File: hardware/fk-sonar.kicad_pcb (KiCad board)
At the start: 2 copper layers, 28.4 x 70.3 mm, 72 parts, among them J1 Conn_01x03, J2 CONN-HDR-2x5, J3 RF-SMA-EDGE, J4 MICRO-USB, J5 S2B-PH-SM4-TB, J6 Conn_01x04, Q1 2N7002LT1G, Q2 2N7002LT1G, Q3 2N7002LT1G, Q4 2N7002LT1G, SW1 SPNO, U1 ATSAMD21G18A-AU, U2 RFM95W, U3 BQ24074RGTT, U4 S25FL116K0XMFI041, U5 MAX1704XX, U6 MCP1700T-3302E/MB, Y1 FC-135

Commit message: New SWD/JTAG programming footprint to avoid confusion.
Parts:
- added M1, M3, M4, M6: MOUNT_HOLE, RocketScreamKicadLibrary:HOLE_NPTH_2.2MM, F.Cu at (141.2, 187.0)
- added M2, M5: FIDUCIAL, RocketScreamKicadLibrary:FIDUCIAL-1MM, F.Cu at (141.2, 187.0)
- J2: footprint Socket_Strips:Socket_Strip_Straight_2x05_Pitch1.27mm_SMD -> conservify:HDR_2x5_Pitch1.27mm_SMD_JTAG_SWD
- moved J2 1.22 mm to (132.3, 119.7), turned to 180 degrees
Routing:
- net 3V3: track 221.8 -> 220.1 mm, vias 17 -> 18
- net GND: track 28.9 -> 27.6 mm
- net /SWDIO: track 20.7 -> 19.9 mm
- net /RST: track 42.9 -> 42.3 mm
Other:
- board text added: "SWD"

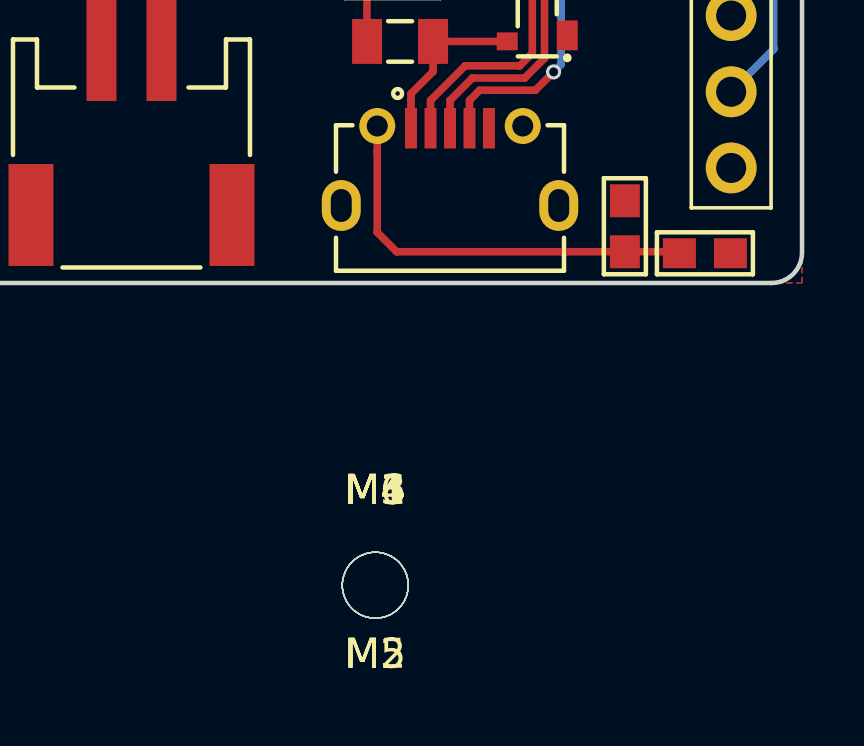
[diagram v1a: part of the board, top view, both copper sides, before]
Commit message: Using our MICRO-USB with the larger, non oval drills.
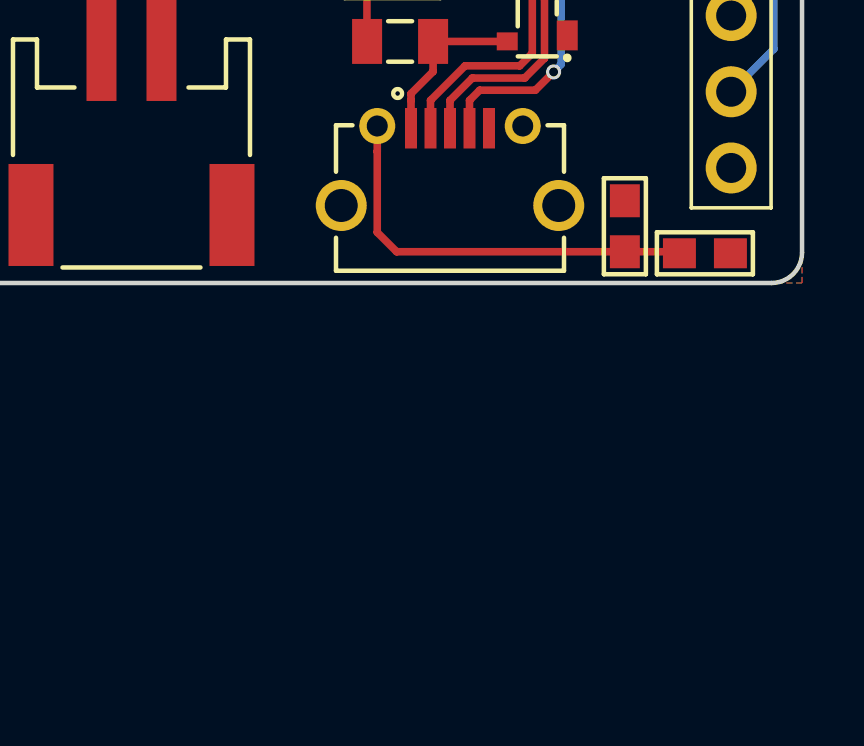
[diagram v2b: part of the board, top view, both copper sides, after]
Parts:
- removed M1, M3, M4, M6: MOUNT_HOLE, RocketScreamKicadLibrary:HOLE_NPTH_2.2MM
- removed M2, M5: FIDUCIAL, RocketScreamKicadLibrary:FIDUCIAL-1MM
- J4: footprint RocketScreamKicadLibrary:MICRO-USB -> conservify:MICRO-USB
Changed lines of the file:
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@@
     (links 179)
     (no_connects 61)
-    (area 118.588857 47.75 165.914286 191.092801)
+    (area 116.859486 47.75 165.914286 191.092801)
     (thickness 1.6)
     (drawings 15)
     (tracks 638)
     (zones 0)
-    (modules 78)
-    (nets 93)
+    (modules 72)
+    (nets 91)
   )
   (page A4)
@@
   (net 89 "Net-(U5-Pad5)")
   (net 90 "Net-(U5-Pad6)")
-  (net 91 "Net-(M2-Pad~)")
-  (net 92 "Net-(M5-Pad~)")
   (net_class Default "This is the default net class."
     (clearance 0.006)
@@
       (net 1 GND))
   )
-  (module RocketScreamKicadLibrary:MICRO-USB (layer F.Cu)
-    (at 143.7132 173.2534)
-    (tags MICRO-USB)
-    (fp_text reference J4 (at 0 -3.556) (layer F.SilkS) hide
-      (effects (font (size 1 1) (thickness 0.15)))
-    )
-    (fp_text value MICRO-USB (at 0 4.318) (layer F.Fab) hide
-      (effects (font (size 1 1) (thickness 0.15)))
-    )
-    (fp_line (start -4.55 -2.4) (end -4.55 3.45) (layer F.CrtYd) (width 0.05))
-    (fp_line (start -4.55 3.45) (end 4.55 3.45) (layer F.CrtYd) (width 0.05))
-    (fp_line (start 4.55 3.45) (end 4.55 -2.4) (layer F.CrtYd) (width 0.05))
-    (fp_line (start 4.55 -2.4) (end -4.55 -2.4) (layer F.CrtYd) (width 0.05))
-    (fp_circle (center -1.746 -2.608) (end -1.796 -2.658) (layer F.SilkS) (width 0.3))
-    (fp_line (start 3.8 0) (end 3.8 -1.55) (layer F.SilkS) (width 0.15))
-    (fp_line (start 3.8 -1.55) (end 3.25 -1.55) (layer F.SilkS) (width 0.15))
-    (fp_line (start -3.8 0) (end -3.8 -1.55) (layer F.SilkS) (width 0.15))
-    (fp_line (start -3.8 -1.55) (end -3.25 -1.55) (layer F.SilkS) (width 0.15))
-    (fp_line (start 3.8 2.2) (end 3.8 3.3) (layer F.SilkS) (width 0.15))
-    (fp_line (start -3.8 3.3) (end -3.8 2.2) (layer F.SilkS) (width 0.15))
-    (fp_line (start -3.8 3.3) (end 3.8 3.3) (layer F.SilkS) (width 0.15))
-    (pad 1 smd rect (at -1.3 -1.45) (size 0.4 1.35) (layers F.Cu F.Paste F.Mask)
-      (net 47 VUSB))
-    (pad 2 smd rect (at -0.65 -1.45) (size 0.4 1.35) (layers F.Cu F.Paste F.Mask)
-      (net 32 /USB-))
-    (pad 3 smd rect (at 0 -1.45) (size 0.4 1.35) (layers F.Cu F.Paste F.Mask)
-      (net 33 /USB+))
-    (pad 4 smd rect (at 0.65 -1.45) (size 0.4 1.35) (layers F.Cu F.Paste F.Mask)
-      (net 71 "Net-(J4-Pad4)"))
-    (pad 5 smd rect (at 1.3 -1.45) (size 0.4 1.35) (layers F.Cu F.Paste F.Mask)
-      (net 1 GND))
-    (pad 6 thru_hole circle (at -2.425 -1.525) (size 1.2 1.2) (drill 0.7) (layers *.Cu *.Mask F.SilkS)
-      (net 57 "Net-(C14-Pad1)"))
-    (pad 7 thru_hole circle (at 2.425 -1.525) (size 1.2 1.2) (drill 0.7) (layers *.Cu *.Mask F.SilkS)
-      (net 72 "Net-(J4-Pad7)"))
-    (pad 8 thru_hole oval (at -3.625 1.125) (size 1.3 1.7) (drill oval 0.7 1.1) (layers *.Cu *.Mask F.SilkS)
-      (net 73 "Net-(J4-Pad8)"))
-    (pad 9 thru_hole oval (at 3.625 1.125) (size 1.3 1.7) (drill oval 0.7 1.1) (layers *.Cu *.Mask F.SilkS)
-      (net 74 "Net-(J4-Pad9)"))
-  )
   (module RocketScreamKicadLibrary:S2B-PH-SM4-TB (layer F.Cu)
     (at 133.096 171.8945)
@@
       (net 2 3V3) (solder_mask_margin 0.1))
   )
-  (module RocketScreamKicadLibrary:HOLE_NPTH_2.2MM (layer F.Cu)
-    (at 141.224 187.036801)
-    (fp_text reference M1 (at 0 -3.175) (layer F.SilkS)
-      (effects (font (size 1 1) (thickness 0.15)))
-    )
-    (fp_text value MOUNT_HOLE (at 0 3.175) (layer F.Fab)
-      (effects (font (size 1 1) (thickness 0.15)))
-    )
-    (pad "" np_thru_hole circle (at 0 0) (size 2.2 2.2) (drill 2.2) (layers *.Cu *.Mask F.SilkS))
-  )
-  (module RocketScreamKicadLibrary:FIDUCIAL-1MM (layer F.Cu)
-    (at 141.224 187.036801)
-    (descr "Circular Fiducial, 1mm bare copper top; 2.54mm keepout")
-    (tags marker)
-    (attr virtual)
-    (fp_text reference M2 (at 0 2.286) (layer F.SilkS)
-      (effects (font (size 1 1) (thickness 0.15)))
-    )
-    (fp_text value FIDUCIAL (at 0 -2.032) (layer F.Fab)
-      (effects (font (size 1 1) (thickness 0.15)))
-    )
-    (pad ~ smd circle (at 0 0) (size 1 1) (layers F.Cu F.Mask)
-      (net 91 "Net-(M2-Pad~)") (solder_mask_margin 0.5) (clearance 0.5))
-  )
-  (module RocketScreamKicadLibrary:HOLE_NPTH_2.2MM (layer F.Cu)
-    (at 141.224 187.036801)
-    (fp_text reference M3 (at 0 -3.175) (layer F.SilkS)
-      (effects (font (size 1 1) (thickness 0.15)))
-    )
-    (fp_text value MOUNT_HOLE (at 0 3.175) (layer F.Fab)
-      (effects (font (size 1 1) (thickness 0.15)))
-    )
-    (pad "" np_thru_hole circle (at 0 0) (size 2.2 2.2) (drill 2.2) (layers *.Cu *.Mask F.SilkS))
-  )
-  (module RocketScreamKicadLibrary:HOLE_NPTH_2.2MM (layer F.Cu)
-    (at 141.224 187.036801)
-    (fp_text reference M4 (at 0 -3.175) (layer F.SilkS)
-      (effects (font (size 1 1) (thickness 0.15)))
-    )
-    (fp_text value MOUNT_HOLE (at 0 3.175) (layer F.Fab)
-      (effects (font (size 1 1) (thickness 0.15)))
-    )
-    (pad "" np_thru_hole circle (at 0 0) (size 2.2 2.2) (drill 2.2) (layers *.Cu *.Mask F.SilkS))
-  )
-  (module RocketScreamKicadLibrary:FIDUCIAL-1MM (layer F.Cu)
-    (at 141.224 187.036801)
-    (descr "Circular Fiducial, 1mm bare copper top; 2.54mm keepout")
-    (tags marker)
-    (attr virtual)
-    (fp_text reference M5 (at 0 2.286) (layer F.SilkS)
-      (effects (font (size 1 1) (thickness 0.15)))
-    )
-    (fp_text value FIDUCIAL (at 0 -2.032) (layer F.Fab)
-      (effects (font (size 1 1) (thickness 0.15)))
-    )
-    (pad ~ smd circle (at 0 0) (size 1 1) (layers F.Cu F.Mask)
-      (net 92 "Net-(M5-Pad~)") (solder_mask_margin 0.5) (clearance 0.5))
-  )
-  (module RocketScreamKicadLibrary:HOLE_NPTH_2.2MM (layer F.Cu)
-    (at 141.224 187.036801)
-    (fp_text reference M6 (at 0 -3.175) (layer F.SilkS)
-      (effects (font (size 1 1) (thickness 0.15)))
+  (module conservify:MICRO-USB (layer F.Cu)
+    (at 143.7132 173.2534)
+    (tags MICRO-USB)
+    (fp_text reference J4 (at -26.162 0) (layer F.SilkS) hide
+      (effects (font (size 0.8 0.8) (thickness 0.15)))
     )
-    (fp_text value MOUNT_HOLE (at 0 3.175) (layer F.Fab)
-      (effects (font (size 1 1) (thickness 0.15)))
+    (fp_text value MICRO-USB (at 0 4.318) (layer F.Fab) hide
+      (effects (font (size 0.8 0.8) (thickness 0.15)))
     )
-    (pad "" np_thru_hole circle (at 0 0) (size 2.2 2.2) (drill 2.2) (layers *.Cu *.Mask F.SilkS))
+    (fp_line (start -4.55 -2.4) (end -4.55 3.45) (layer F.CrtYd) (width 0.05))
+    (fp_line (start -4.55 3.45) (end 4.55 3.45) (layer F.CrtYd) (width 0.05))
+    (fp_line (start 4.55 3.45) (end 4.55 -2.4) (layer F.CrtYd) (width 0.05))
+    (fp_line (start 4.55 -2.4) (end -4.55 -2.4) (layer F.CrtYd) (width 0.05))
+    (fp_circle (center -1.746 -2.608) (end -1.796 -2.658) (layer F.SilkS) (width 0.3))
+    (fp_line (start 3.8 0) (end 3.8 -1.55) (layer F.SilkS) (width 0.15))
+    (fp_line (start 3.8 -1.55) (end 3.25 -1.55) (layer F.SilkS) (width 0.15))
+    (fp_line (start -3.8 0) (end -3.8 -1.55) (layer F.SilkS) (width 0.15))
+    (fp_line (start -3.8 -1.55) (end -3.25 -1.55) (layer F.SilkS) (width 0.15))
+    (fp_line (start 3.8 2.2) (end 3.8 3.3) (layer F.SilkS) (width 0.15))
+    (fp_line (start -3.8 3.3) (end -3.8 2.2) (layer F.SilkS) (width 0.15))
+    (fp_line (start -3.8 3.3) (end 3.8 3.3) (layer F.SilkS) (width 0.15))
+    (pad 1 smd rect (at -1.3 -1.45) (size 0.4 1.35) (layers F.Cu F.Paste F.Mask)
+      (net 47 VUSB))
+    (pad 2 smd rect (at -0.65 -1.45) (size 0.4 1.35) (layers F.Cu F.Paste F.Mask)
+      (net 32 /USB-))
+    (pad 3 smd rect (at 0 -1.45) (size 0.4 1.35) (layers F.Cu F.Paste F.Mask)
+      (net 33 /USB+))
+    (pad 4 smd rect (at 0.65 -1.45) (size 0.4 1.35) (layers F.Cu F.Paste F.Mask)
+      (net 71 "Net-(J4-Pad4)"))
+    (pad 5 smd rect (at 1.3 -1.45) (size 0.4 1.35) (layers F.Cu F.Paste F.Mask)
+      (net 1 GND))
+    (pad 6 thru_hole circle (at -2.425 -1.525) (size 1.2 1.2) (drill 0.7) (layers *.Cu *.Mask F.Paste)
+      (net 57 "Net-(C14-Pad1)"))
+    (pad 7 thru_hole circle (at 2.425 -1.525) (size 1.2 1.2) (drill 0.7) (layers *.Cu *.Mask F.Paste)
+      (net 72 "Net-(J4-Pad7)"))
+    (pad 8 thru_hole circle (at -3.625 1.125) (size 1.7 1.7) (drill oval 1.1) (layers *.Cu *.Mask F.Paste)
+      (net 73 "Net-(J4-Pad8)"))
+    (pad 9 thru_hole circle (at 3.625 1.125) (size 1.7 1.7) (drill oval 1.1) (layers *.Cu *.Mask F.Paste)
+      (net 74 "Net-(J4-Pad9)"))
   )
   (gr_text SWD (at 128.27 119.6975 90) (layer F.SilkS)

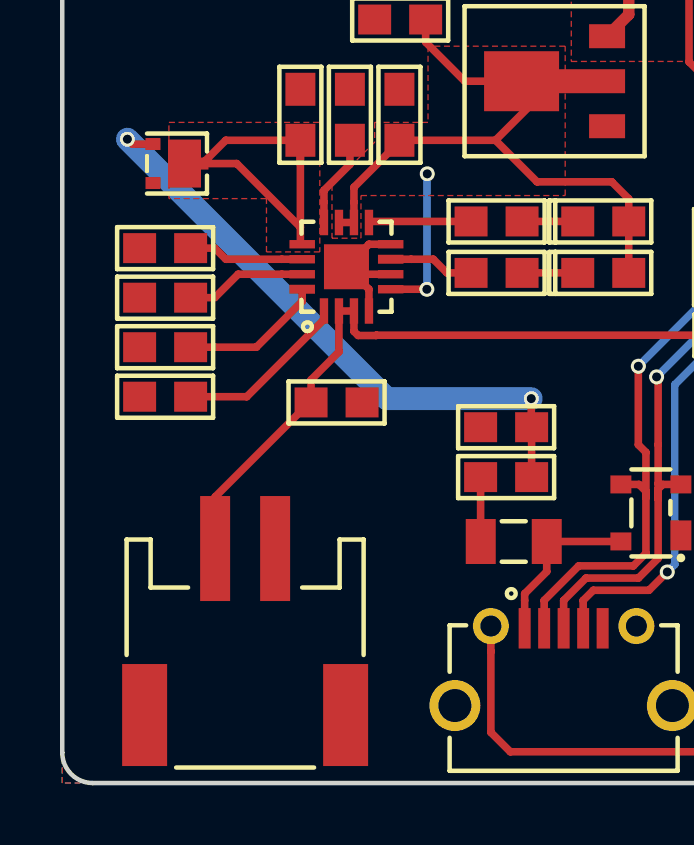
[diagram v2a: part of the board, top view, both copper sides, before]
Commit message: Adding a solar panel connector. Just a JST below the battery JST.
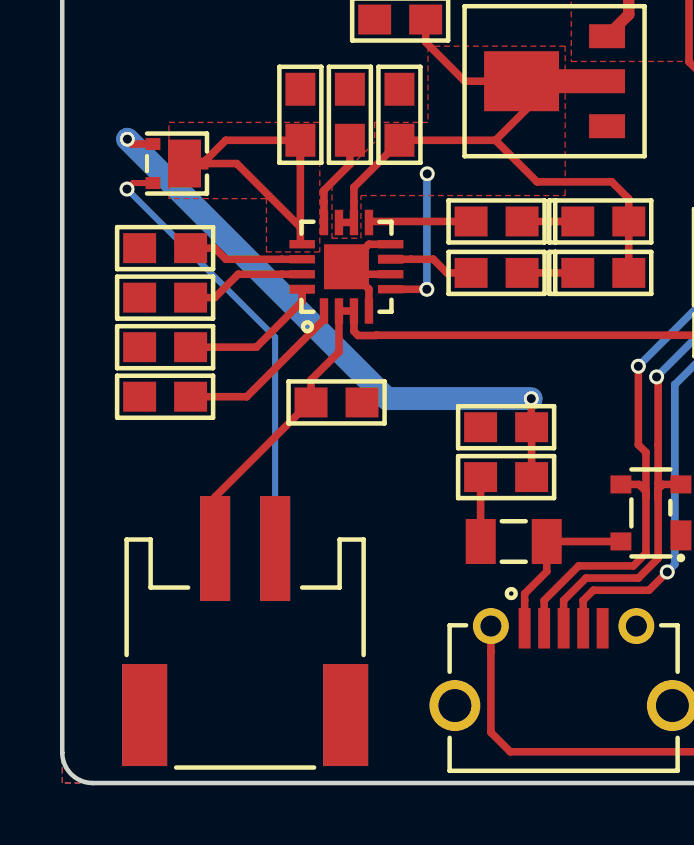
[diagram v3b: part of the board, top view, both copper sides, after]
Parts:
- added J7: S2B-PH-SM4-TB, RocketScreamKicadLibrary:S2B-PH-SM4-TB, B.Cu at (133.1, 171.9)
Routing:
- net VIN: track 0.00 -> 15.0 mm, vias 0 -> 1
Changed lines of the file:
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@@
 (kicad_pcb (version 4) (host pcbnew 4.0.7-e2-6376~58~ubuntu16.04.1)
   (general
-    (links 179)
-    (no_connects 61)
-    (area 116.859486 47.75 165.914286 191.092801)
+    (links 181)
+    (no_connects 0)
+    (area 126.924999 106.604999 155.523001 177.036801)
     (thickness 1.6)
     (drawings 15)
-    (tracks 638)
+    (tracks 643)
     (zones 0)
-    (modules 72)
-    (nets 91)
+    (modules 73)
+    (nets 93)
   )
   (page A4)
@@
   )
   (setup
-    (last_trace_width 0.006)
+    (last_trace_width 0.2032)
     (user_trace_width 0.2032)
     (user_trace_width 0.254)
@@
   (net 89 "Net-(U5-Pad5)")
   (net 90 "Net-(U5-Pad6)")
+  (net 91 "Net-(J7-Pad3)")
+  (net 92 "Net-(J7-Pad4)")
   (net_class Default "This is the default net class."
     (clearance 0.006)
@@
     (add_net "Net-(J5-Pad3)")
     (add_net "Net-(J5-Pad4)")
-    (add_net "Net-(M2-Pad~)")
-    (add_net "Net-(M5-Pad~)")
+    (add_net "Net-(J7-Pad3)")
+    (add_net "Net-(J7-Pad4)")
     (add_net "Net-(Q1-Pad3)")
     (add_net "Net-(Q2-Pad3)")
@@
       (net 74 "Net-(J4-Pad9)"))
   )
+  (module RocketScreamKicadLibrary:S2B-PH-SM4-TB (layer B.Cu)
+    (at 133.096 171.8945 180)
+    (tags "JST PH")
+    (fp_text reference J7 (at 0 5.588 180) (layer B.SilkS) hide
+      (effects (font (size 1 1) (thickness 0.15)) (justify mirror))
+    )
+    (fp_text value S2B-PH-SM4-TB (at 0 -5.842 180) (layer B.Fab) hide
+      (effects (font (size 1 1) (thickness 0.15)) (justify mirror))
+    )
+    (fp_line (start -4.35 -4.8) (end -4.35 4.8) (layer B.CrtYd) (width 0.05))
+    (fp_line (start -4.35 4.8) (end 4.35 4.8) (layer B.CrtYd) (width 0.05))
+    (fp_line (start 4.35 4.8) (end 4.35 -4.8) (layer B.CrtYd) (width 0.05))
+    (fp_line (start -4.35 -4.8) (end 4.35 -4.8) (layer B.CrtYd) (width 0.05))
+    (fp_line (start 3.15 1.45) (end 3.15 3.05) (layer B.SilkS) (width 0.15))
+    (fp_line (start 3.15 3.05) (end 3.95 3.05) (layer B.SilkS) (width 0.15))
+    (fp_line (start 3.95 3.05) (end 3.95 -0.8) (layer B.SilkS) (width 0.15))
+    (fp_line (start -2.3 -4.55) (end 2.3 -4.55) (layer B.SilkS) (width 0.15))
+    (fp_line (start -3.15 1.45) (end -3.15 3.05) (layer B.SilkS) (width 0.15))
+    (fp_line (start -3.15 3.05) (end -3.95 3.05) (layer B.SilkS) (width 0.15))
+    (fp_line (start -3.95 3.05) (end -3.95 -0.8) (layer B.SilkS) (width 0.15))
+    (fp_line (start 3.15 1.45) (end 1.9 1.45) (layer B.SilkS) (width 0.15))
+    (fp_line (start -3.15 1.45) (end -1.9 1.45) (layer B.SilkS) (width 0.15))
+    (pad 1 smd rect (at -1 2.75 180) (size 1 3.5) (layers B.Cu B.Paste B.Mask)
+      (net 63 VIN))
+    (pad 2 smd rect (at 1 2.75 180) (size 1 3.5) (layers B.Cu B.Paste B.Mask)
+      (net 1 GND))
+    (pad 3 smd rect (at -3.35 -2.8 180) (size 1.5 3.4) (layers B.Cu B.Paste B.Mask)
+      (net 91 "Net-(J7-Pad3)"))
+    (pad 4 smd rect (at 3.35 -2.8 180) (size 1.5 3.4) (layers B.Cu B.Paste B.Mask)
+      (net 92 "Net-(J7-Pad4)"))
+  )
   (gr_text SWD (at 128.27 119.6975 90) (layer F.SilkS)
     (effects (font (size 1 1) (thickness 0.2)))
@@
   (segment (start 151.757661 161.271381) (end 152.519661 162.033381) (width 0.254) (layer F.Cu) (net 61))
   (segment (start 139.456285 108.040537) (end 137.043285 108.040537) (width 0.2032) (layer F.Cu) (net 62))
+  (segment (start 129.159 157.1625) (end 134.096 162.0995) (width 0.2032) (layer B.Cu) (net 63))
+  (segment (start 134.096 162.0995) (end 134.096 169.1445) (width 0.2032) (layer B.Cu) (net 63))
+  (segment (start 130.0248 156.9616) (end 129.3599 156.9616) (width 0.2032) (layer F.Cu) (net 63))
+  (segment (start 129.3599 156.9616) (end 129.159 157.1625) (width 0.2032) (layer F.Cu) (net 63))
+  (via (at 129.159 157.1625) (size 0.5) (drill 0.3) (layers F.Cu B.Cu) (net 63))
   (segment (start 144.184 159.9565) (end 142.328 159.9565) (width 0.254) (layer F.Cu) (net 64))
   (segment (start 142.328 158.242) (end 144.184 158.242) (width 0.254) (layer F.Cu) (net 65))
